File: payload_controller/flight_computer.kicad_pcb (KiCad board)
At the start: 4 copper layers, 87 x 75 mm, 154 parts, among them J1 GaAs Cell, J2 G125-MH12605M4R, J3 Conn_01x08_Female, J4 Conn_02x07_Odd_Even, J5 0781710004, J6 Conn_01x03_Male, J7 GaAs Temp, Q1 DMC2053UVT, U1 74HC590, U10 OPA2387, U11 MCP4725xxx-xCH, U12 ADS131M04IPWR, U13 INA190A4IDDFR, U14 74LVC1G332, U15 SN74LVC1G14DRL, U16 CD4518BM96, U17 CD4028BMT, U18 CD4028BMT, U19 MAX4736EUBT, U2 ADG841YKSZ-500RL7, U20 MAX4736EUBT, U21 MAX4736EUBT, U22 MAX4736EUBT, U23 MAX4736EUBT, U24 MAX4736EUBT, U25 MAX4736EUBT, U26 MAX4736EUBT, U27 MAX4736EUBT, U28 MAX4736EUBT, U29 MAX4736EUBT, U3 ADG841YKSZ-500RL7, U30 LT3092EDD#TRPBF, U31 LT6654AMPS6-1.25, U33 ICL7660CSAT, U34 MSP430FR5969IRGZR, U4 ADG841YKSZ-500RL7, U5 ADG841YKSZ-500RL7, U6 ADG841YKSZ-500RL7, U7 ADG841YKSZ-500RL7, U8 ADG841YKSZ-500RL7, U9 ADG841YKSZ-500RL7, X1 CB3LV-3I-8M1920, Y1 CM8V-T1A

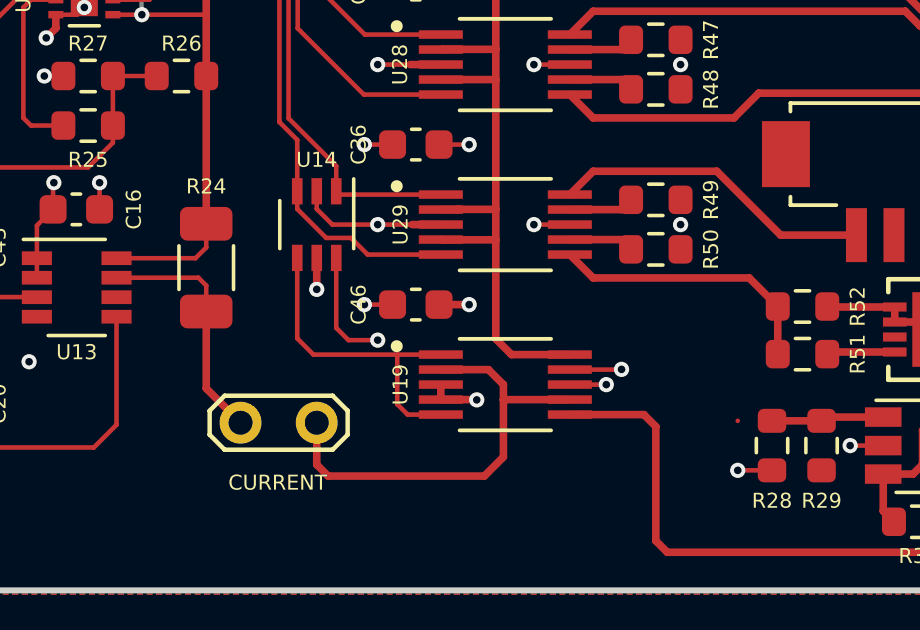
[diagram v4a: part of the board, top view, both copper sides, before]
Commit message: Update disconnected trace, regenerate
- Delete extra projects
- Package gerbers
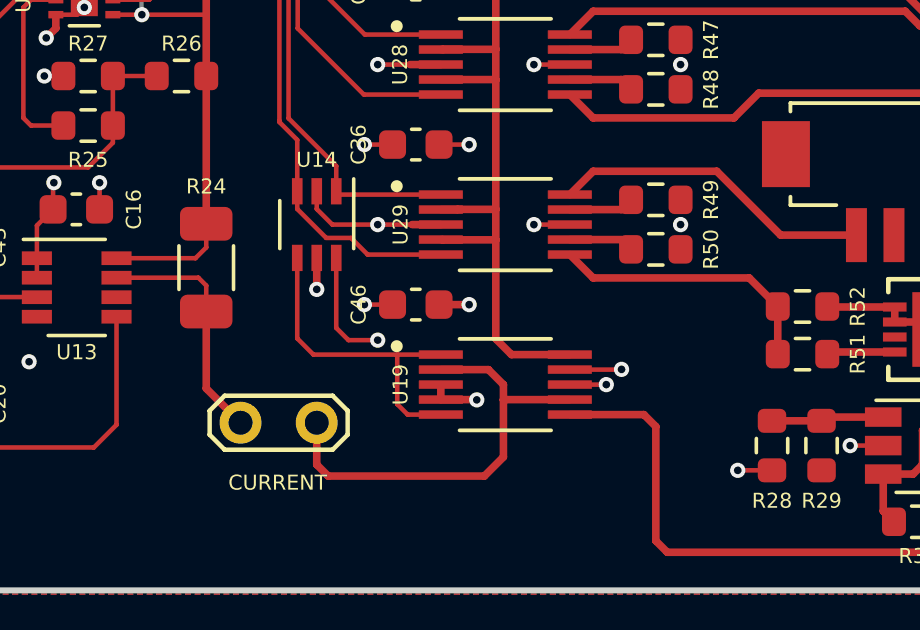
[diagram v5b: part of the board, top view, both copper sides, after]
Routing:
- net /Payload Controller/ENABLE_TEST_SOURCE: track 106.0 -> 107.2 mm
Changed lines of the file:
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@@
     (thickness 1.6)
     (drawings 19)
-    (tracks 1652)
+    (tracks 1648)
     (zones 0)
     (modules 154)
@@
     (38 B.Mask user)
     (39 F.Mask user)
-    (40 Dwgs.User user)
+    (40 Dwgs.User user hide)
     (41 Cmts.User user hide)
     (42 Eco1.User user)
@@
       (excludeedgelayer true)
       (linewidth 0.100000)
-      (plotframeref false)
+      (plotframeref true)
       (viasonmask false)
       (mode 1)
@@
       (padsonsilk false)
       (subtractmaskfromsilk false)
-      (outputformat 1)
+      (outputformat 4)
       (mirror false)
       (drillshape 0)
       (scaleselection 1)
-      (outputdirectory "gerbers"))
+      (outputdirectory "renders"))
   )
   (net 0 "")
@@
       (effects (font (size 0.8 0.8) (thickness 0.12)))
     )
-    (pad 2 smd roundrect (at 1.4625 0 270) (size 1.125 1.75) (layers F.Cu F.Paste F.Mask) (roundrect_rratio 0.2222213333333333)
+    (pad 2 smd roundrect (at 1.4625 0 270) (size 1.125 1.75) (layers F.Cu F.Paste F.Mask) (roundrect_rratio 0.2222204444444444)
       (net 180 "Net-(R24-Pad2)"))
-    (pad 1 smd roundrect (at -1.4625 0 270) (size 1.125 1.75) (layers F.Cu F.Paste F.Mask) (roundrect_rratio 0.2222213333333333)
+    (pad 1 smd roundrect (at -1.4625 0 270) (size 1.125 1.75) (layers F.Cu F.Paste F.Mask) (roundrect_rratio 0.2222204444444444)
       (net 50 "/Curve Tracer/LADDER_VOLTAGE"))
     (model ${KISYS3DMOD}/Resistor_SMD.3dshapes/R_1206_3216Metric.wrl
@@
   (segment (start 153.924 120.142) (end 154.178 120.396) (width 0.1524) (layer F.Cu) (net 61))
   (via (at 177.7365 131.8895) (size 0.508) (drill 0.254) (layers F.Cu B.Cu) (net 62))
-  (segment (start 177.737 130.238) (end 177.7365 130.2385) (width 0.1524) (layer F.Cu) (net 62))
   (segment (start 178.8795 131.889) (end 177.737 131.889) (width 0.1524) (layer F.Cu) (net 62))
-  (segment (start 177.7365 133.07057) (end 177.2285 133.57857) (width 0.1524) (layer In2.Cu) (net 62))
-  (segment (start 177.2285 133.57857) (end 135.21382 133.57857) (width 0.1524) (layer In2.Cu) (net 62))
-  (segment (start 135.21382 133.57857) (end 128.140768 133.57857) (width 0.1524) (layer In2.Cu) (net 62))
-  (segment (start 128.140768 133.57857) (end 127.68581 133.123612) (width 0.1524) (layer In2.Cu) (net 62))
-  (segment (start 127.68581 133.123612) (end 127.68581 119.38) (width 0.1524) (layer In2.Cu) (net 62))
-  (segment (start 127.68581 114.527132) (end 128.041411 114.171531) (width 0.1524) (layer In2.Cu) (net 62))
-  (segment (start 127.68581 119.38) (end 127.68581 114.527132) (width 0.1524) (layer In2.Cu) (net 62))
-  (segment (start 128.041411 114.171531) (end 128.041411 113.538) (width 0.1524) (layer In2.Cu) (net 62))
-  (segment (start 128.041409 111.608343) (end 127.86362 111.430554) (width 0.1524) (layer In2.Cu) (net 62))
-  (segment (start 128.041411 113.538) (end 128.041409 111.608343) (width 0.1524) (layer In2.Cu) (net 62))
-  (segment (start 127.86362 111.430554) (end 127.66043 111.227364) (width 0.1524) (layer In2.Cu) (net 62))
-  (segment (start 127.66043 111.227364) (end 127.66043 89.82707) (width 0.1524) (layer In2.Cu) (net 62))
-  (segment (start 127.66043 89.82707) (end 128.7145 88.773) (width 0.1524) (layer In2.Cu) (net 62))
   (via (at 128.906357 87.51735) (size 0.508) (drill 0.254) (layers F.Cu B.Cu) (net 62))
-  (segment (start 128.7145 87.709207) (end 128.906357 87.51735) (width 0.1524) (layer In2.Cu) (net 62))
-  (segment (start 128.7145 88.773) (end 128.7145 87.709207) (width 0.1524) (layer In2.Cu) (net 62))
   (segment (start 127.512 82.572932) (end 127.512 80.7145) (width 0.1524) (layer F.Cu) (net 62))
   (segment (start 127.0889 82.996032) (end 127.512 82.572932) (width 0.1524) (layer F.Cu) (net 62))
@@
   (segment (start 128.41135 87.51735) (end 127.0889 86.1949) (width 0.1524) (layer F.Cu) (net 62))
   (segment (start 128.906357 87.51735) (end 128.41135 87.51735) (width 0.1524) (layer F.Cu) (net 62))
+  (segment (start 177.7365 133.07057) (end 177.7365 131.8895) (width 0.1524) (layer In2.Cu) (net 62))
+  (segment (start 177.2285 133.57857) (end 177.7365 133.07057) (width 0.1524) (layer In2.Cu) (net 62))
+  (segment (start 128.140768 133.57857) (end 177.2285 133.57857) (width 0.1524) (layer In2.Cu) (net 62))
+  (segment (start 127.68581 133.123612) (end 128.140768 133.57857) (width 0.1524) (layer In2.Cu) (net 62))
+  (segment (start 127.68581 114.527132) (end 127.68581 133.123612) (width 0.1524) (layer In2.Cu) (net 62))
+  (segment (start 128.041411 114.171531) (end 127.68581 114.527132) (width 0.1524) (layer In2.Cu) (net 62))
+  (segment (start 127.66043 111.227364) (end 128.041409 111.608343) (width 0.1524) (layer In2.Cu) (net 62))
+  (segment (start 128.7145 88.773) (end 127.66043 89.82707) (width 0.1524) (layer In2.Cu) (net 62))
+  (segment (start 128.7145 87.709207) (end 128.7145 88.773) (width 0.1524) (layer In2.Cu) (net 62))
+  (segment (start 128.041409 111.608343) (end 128.041411 114.171531) (width 0.1524) (layer In2.Cu) (net 62))
+  (segment (start 127.66043 89.82707) (end 127.66043 111.227364) (width 0.1524) (layer In2.Cu) (net 62))
+  (segment (start 128.906357 87.51735) (end 128.7145 87.709207) (width 0.1524) (layer In2.Cu) (net 62))
   (segment (start 173.8555 75.192) (end 174.181 74.8665) (width 0.254) (layer F.Cu) (net 63))
   (segment (start 172.123 75.192) (end 173.8555 75.192) (width 0.254) (layer F.Cu) (net 63))
